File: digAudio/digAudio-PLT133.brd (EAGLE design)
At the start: 18.4 x 37.5 mm, 12 parts

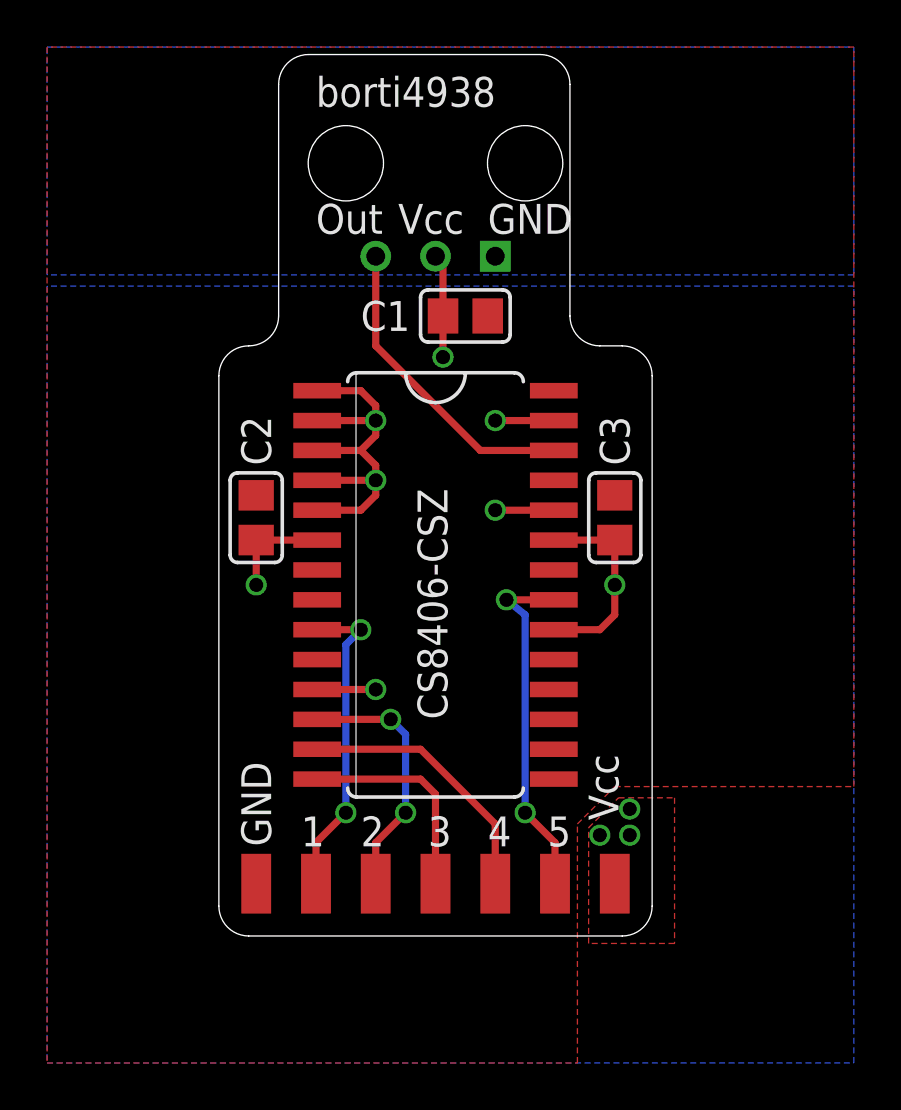
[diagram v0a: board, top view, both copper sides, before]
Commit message: Update PCBs incl. the DRC and add a new version with an optical jack available at digikey
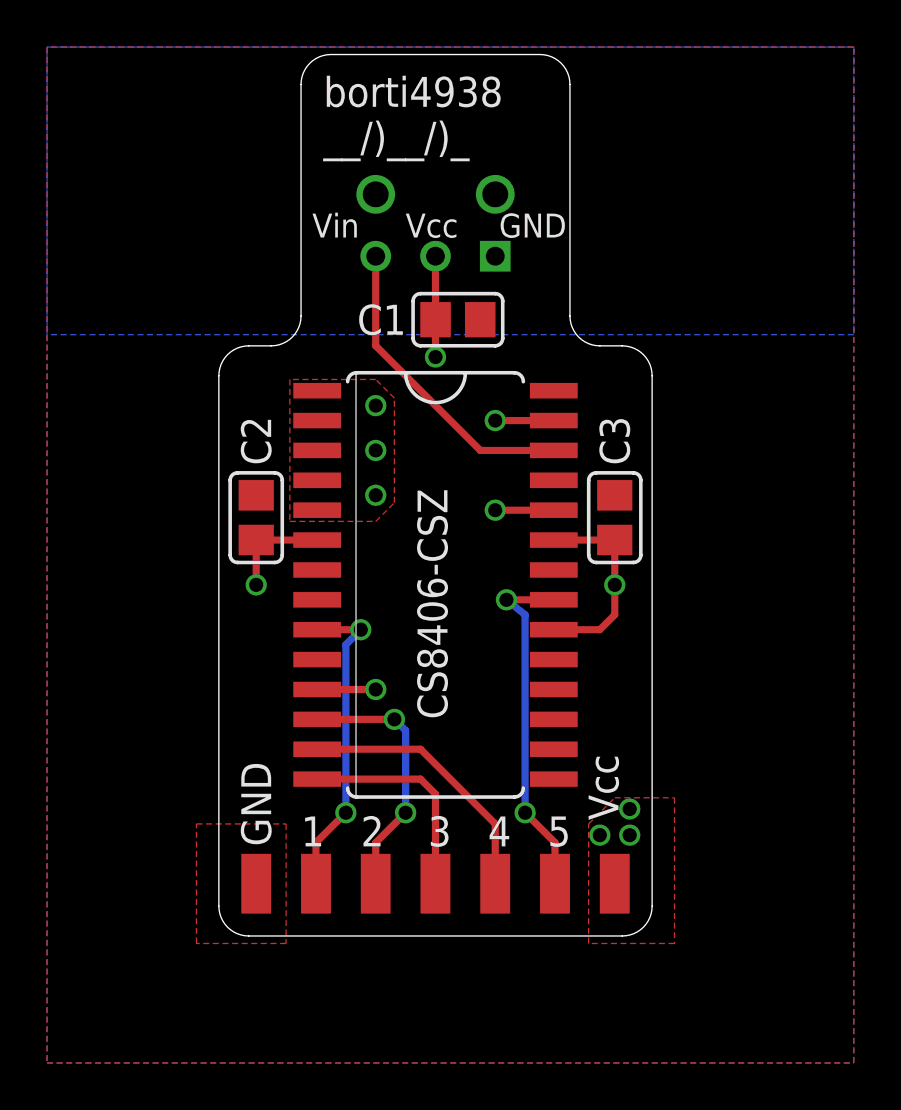
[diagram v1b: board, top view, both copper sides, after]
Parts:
- removed U$2: PHOTOLINK, cs8406:PHOTOLONK
- added U$6: PLT133/T10W, cs8406:PLT133/T10W
- moved U$5 0.35 mm to (17.5, 31.6)
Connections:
- net GND: now also U$6.P$1; no longer U$2.P$1
- net N$1: now also U$6.P$3; no longer U$2.P$3
- net VCC: now also U$6.P$2; no longer U$2.P$2
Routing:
- net VCC: track 41.7 -> 25.2 mm, vias 11 -> 12
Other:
- outline, holes or cut-outs redrawn
- board text added: "Vin"
- board text added: "borti4938 __/)__/)_"
- board text removed: "Out"
- board text removed: "borti4938"
